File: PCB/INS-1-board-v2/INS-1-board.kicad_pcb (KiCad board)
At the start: 2 copper layers, 11 parts, among them J1 Conn_3_screw_OSTVN03A150, Q1 MPSA42, Q2 MPSA42

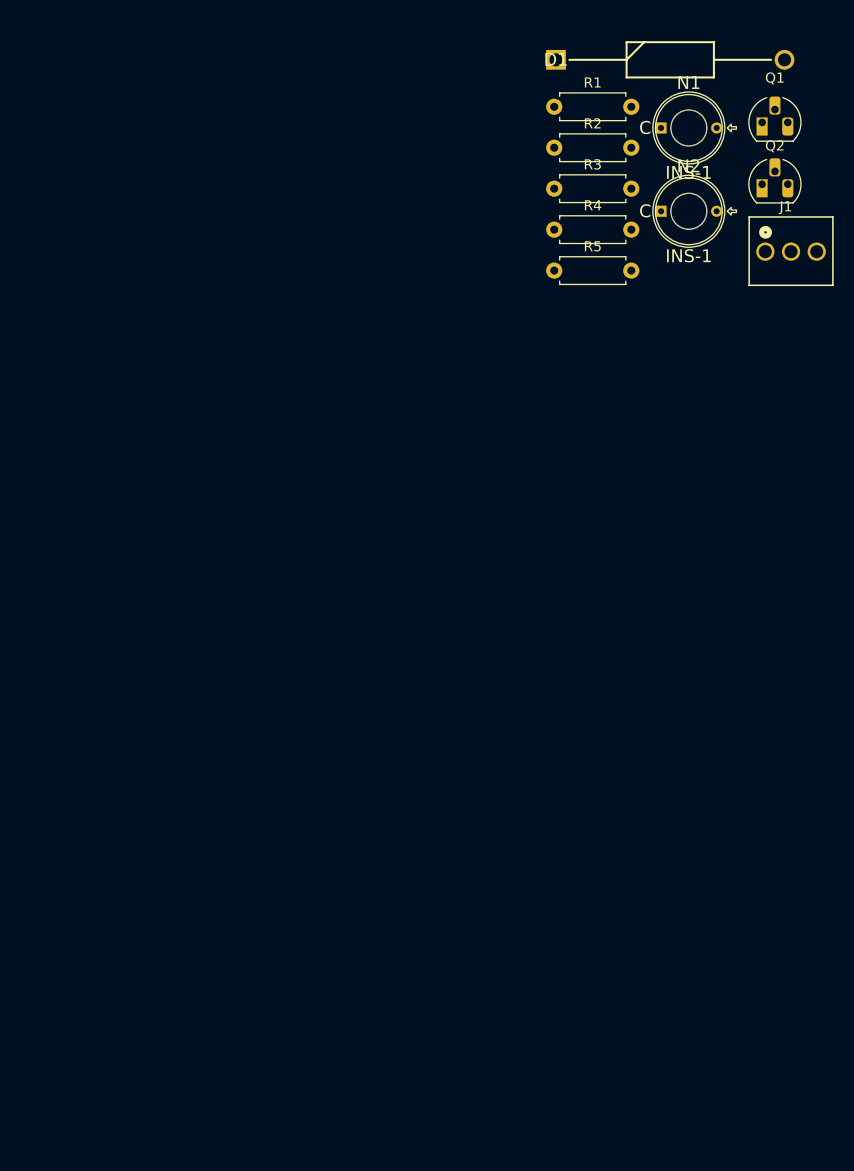
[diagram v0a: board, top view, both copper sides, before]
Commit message: Moved docs to hv-ps-docs for the claude swe framework
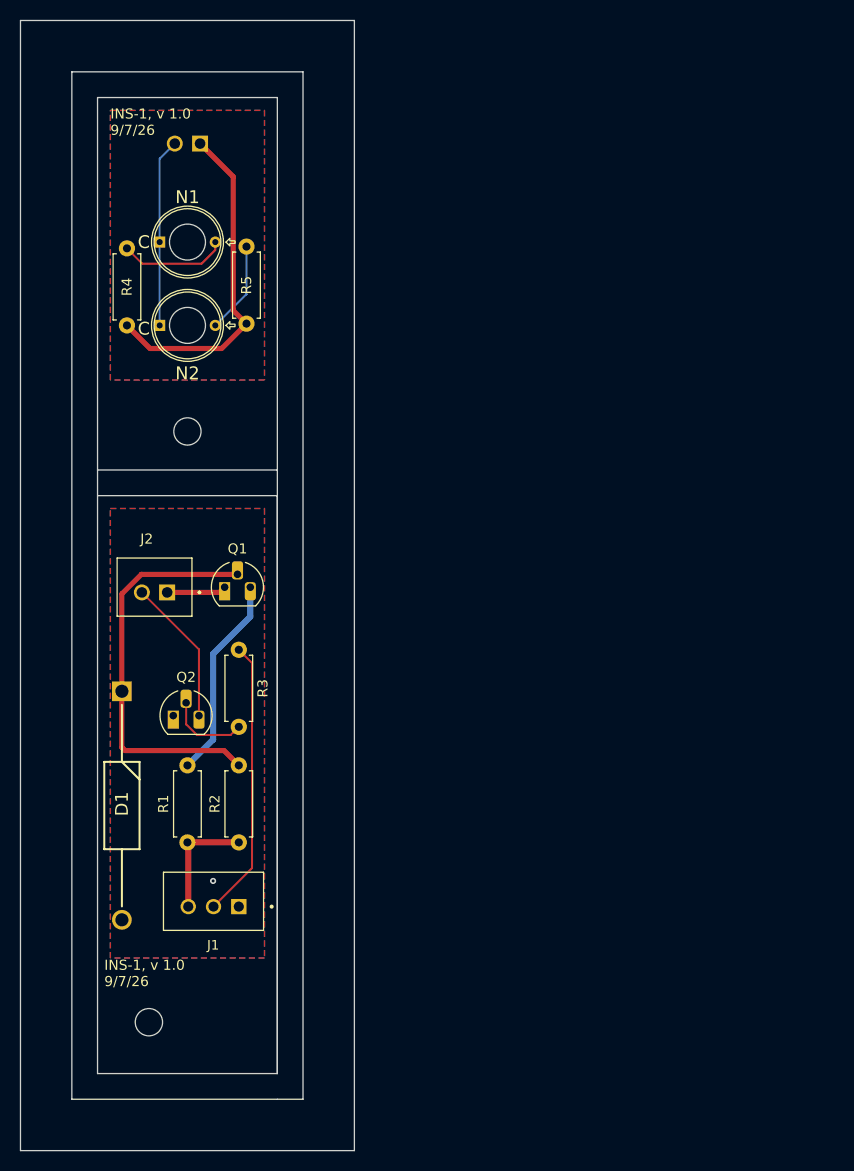
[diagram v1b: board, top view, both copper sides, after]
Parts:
- added H1: MountingHole, MountingHole:MountingHole_2.7mm, F.Cu at (61.0, 174.0)
- added H2: MountingHole, MountingHole:MountingHole_2.7mm, F.Cu at (64.8, 115.6)
- added J2: B2B-XH-A, INS-1-footprints:JST_B2B-XH-A, F.Cu at (61.5, 131.0)
- added J3: B2B-XH-A, INS-1-footprints:JST_B2B-XH-A, B.Cu at (64.8, 87.6)
- D1: footprint HV-PS-555:DIOAD2260W109L864D349 -> INS-1-footprints:DIOAD2260W109L864D349
- J1: value Conn_3_screw_OSTVN03A150 -> B3B-XH-A; footprint nixie-footprints:CONN3_OSTVN03A150_OST -> INS-1-footprints:JST_B3B-XH-A
- Q1: footprint Package_TO_SOT_THT:TO-92_HandSolder -> INS-1-footprints:TO-92L_HandSolder
- R1: value 100K -> 10K; footprint Resistor_THT:R_Axial_DIN0207_L6.3mm_D2.5mm_P7.62mm_Horizontal -> INS-1-footprints:R_Axial_DIN0207_L6.3mm_D2.5mm_P7.62mm_Horizontal
- R2: value 10K -> 100K; footprint Resistor_THT:R_Axial_DIN0207_L6.3mm_D2.5mm_P7.62mm_Horizontal -> INS-1-footprints:R_Axial_DIN0207_L6.3mm_D2.5mm_P7.62mm_Horizontal
- R3: value 100k -> 10K; footprint Resistor_THT:R_Axial_DIN0207_L6.3mm_D2.5mm_P7.62mm_Horizontal -> INS-1-footprints:R_Axial_DIN0207_L6.3mm_D2.5mm_P7.62mm_Horizontal
- R4: value 10K -> 100k; footprint Resistor_THT:R_Axial_DIN0207_L6.3mm_D2.5mm_P7.62mm_Horizontal -> INS-1-footprints:R_Axial_DIN0207_L6.3mm_D2.5mm_P7.62mm_Horizontal
- R5: footprint Resistor_THT:R_Axial_DIN0207_L6.3mm_D2.5mm_P7.62mm_Horizontal -> INS-1-footprints:R_Axial_DIN0207_L6.3mm_D2.5mm_P7.62mm_Horizontal
- moved J1 84.3 mm to (67.3, 162.0)
- moved R1 81.3 mm to (64.8, 156.2), turned to 90 degrees
- moved Q2 78.4 mm to (63.4, 143.7)
- moved D1 75.8 mm to (58.3, 141.3), turned to -90 degrees
- moved R2 75.4 mm to (69.8, 156.2), turned to 90 degrees
- moved Q1 70.3 mm to (68.4, 131.0)
- moved R3 55.2 mm to (69.8, 137.2), turned to -90 degrees
- moved N1 50.8 mm to (64.8, 96.8)
- moved N2 50.8 mm to (64.8, 105.1)
- moved R4 43.3 mm to (58.8, 105.1), turned to 90 degrees
- moved R5 30.9 mm to (70.6, 104.9), turned to 90 degrees
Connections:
- net HV renamed Net-(J1-Pad3)
- J1 pad 1: CNTRL -> GND
- J1 pad 2: GND -> Net-(J1-Pad2)
- Q1 pad 1: 90V -> Net-(Q1-E)
- Q2 pad 3: Net-(N1-C) -> Net-(Q2-C)
- R1 pad 2: Net-(D1-K) -> Net-(Q1-C)
- R2 pad 2: Net-(Q1-C) -> Net-(D1-K)
- R3 pad 1: 90V -> Net-(J1-Pad2)
- R3 pad 2: Net-(N1-A) -> Net-(Q2-B)
- R4 pad 1: CNTRL -> Net-(J3-Pad1)
- R4 pad 2: Net-(Q2-B) -> Net-(N1-A)
- R5 pad 1: 90V -> Net-(J3-Pad1)
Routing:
- net Net-(D1-K): track 0.00 -> 39.7 mm
- net Net-(J3-Pad1): track 0.00 -> 33.5 mm
- net Net-(J1-Pad2): track 0.00 -> 27.5 mm
- net Net-(Q1-C): track 0.00 -> 20.2 mm
- net Net-(N1-C): track 0.00 -> 18.6 mm
- net Net-(Q2-C): track 0.00 -> 14.5 mm
- net Net-(J1-Pad3): track 0.00 -> 11.5 mm
- net Net-(N1-A): track 0.00 -> 10.7 mm
- net Net-(N2-A): track 0.00 -> 9.07 mm
- net Net-(Q2-B): track 0.00 -> 8.10 mm
- net Net-(Q1-E): track 0.00 -> 5.90 mm
- net GND: vias 0 -> 1
- added copper zone on B.Cu, net GND
- added copper zone on F.Cu, net GND
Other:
- board outline added: 33 x 111.8 mm
- board text added: "INS-1, v 1.0 9/7/26"
- board text added: "James Gallager"
- board text added: "This is a 'panelized' board, to be sent to OSH Park. The interior edge cuts will be made except that the two boards will be joined by a single tab with 'mouse bite' holes. The two boards are separated by a 0.1{dblquote} boundary and the set of baords is withing a 0.2{dblquote} frame."
